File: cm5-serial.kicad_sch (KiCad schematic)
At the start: 1 part

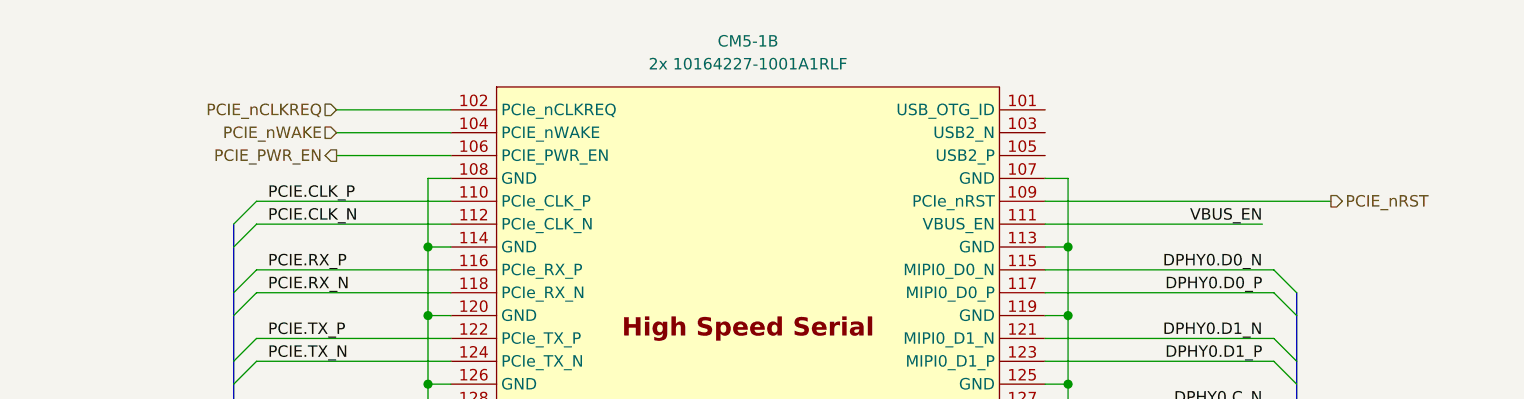
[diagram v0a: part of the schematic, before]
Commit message: abstractified pcie sideband sigs
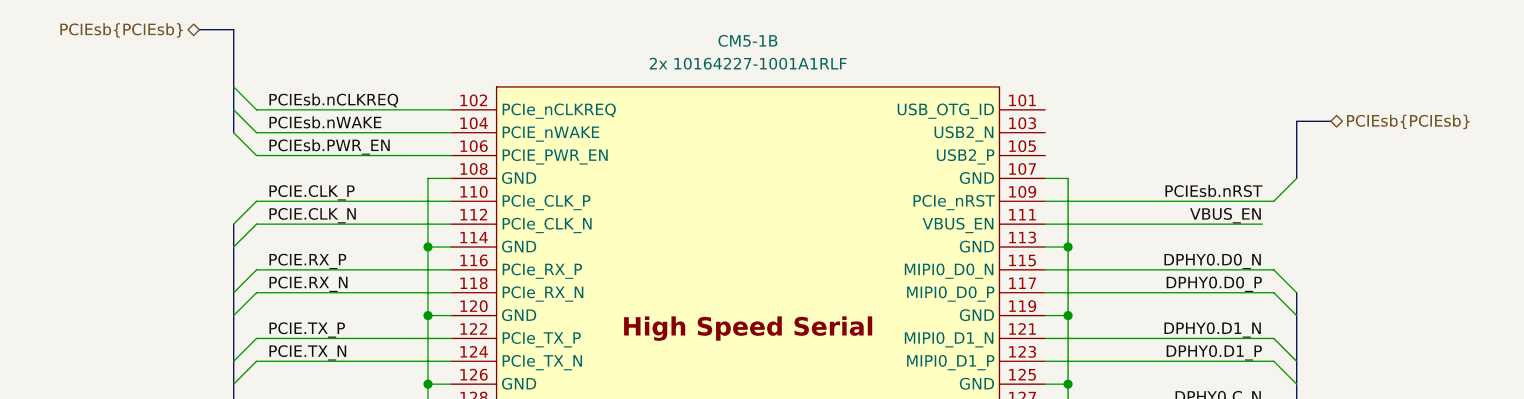
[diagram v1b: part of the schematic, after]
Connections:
- net PCIE_PWR_EN renamed PCIEsb.PWR_EN
- net PCIE_nCLKREQ renamed PCIEsb.nCLKREQ
- net PCIE_nRST renamed PCIEsb.nRST
- net PCIE_nWAKE renamed PCIEsb.nWAKE
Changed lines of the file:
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@@
 		(company "Andre S Winkel | Highlander Space Program | University of California, Riverside")
+	)
+	(bus_alias "PCIEsb"
+		(members "nCLKREQ" "nWAKE" "PWR_EN" "nRST")
 	)
 	(junction
@@
 	)
 	(bus_entry
+		(at 74.93 34.29)
+		(size 2.54 2.54)
+		(stroke
+			(width 0)
+			(type default)
+		)
+	)
+	(bus_entry
 		(at 74.93 44.45)
 		(size 2.54 -2.54)
@@
 	)
 	(bus_entry
+		(at 193.04 39.37)
+		(size -2.54 2.54)
+		(stroke
+			(width 0)
+			(type default)
+		)
+	)
+	(bus_entry
+		(at 74.93 29.21)
+		(size 2.54 2.54)
+		(stroke
+			(width 0)
+			(type default)
+		)
+	)
+	(bus_entry
 		(at 193.04 77.47)
 		(size -2.54 -2.54)
@@
 	)
 	(bus_entry
+		(at 77.47 34.29)
+		(size -2.54 -2.54)
+		(stroke
+			(width 0)
+			(type default)
+		)
+	)
+	(bus_entry
 		(at 193.04 151.13)
 		(size -2.54 -2.54)
@@
 	(wire
 		(pts
-			(xy 86.36 36.83) (xy 99.06 36.83)
-		)
-		(stroke
-			(width 0)
-			(type default)
-		)
-	)
-	(wire
-		(pts
 			(xy 167.64 62.23) (xy 167.64 54.61)
 		)
@@
 	(wire
 		(pts
+			(xy 77.47 36.83) (xy 99.06 36.83)
+		)
+		(stroke
+			(width 0)
+			(type default)
+		)
+	)
+	(wire
+		(pts
 			(xy 167.64 153.67) (xy 167.64 161.29)
 		)
@@
 		)
 	)
+	(bus
+		(pts
+			(xy 74.93 22.86) (xy 71.12 22.86)
+		)
+		(stroke
+			(width 0)
+			(type default)
+		)
+	)
 	(wire
 		(pts
@@
 	(bus
 		(pts
+			(xy 193.04 33.02) (xy 193.04 39.37)
+		)
+		(stroke
+			(width 0)
+			(type default)
+		)
+	)
+	(bus
+		(pts
 			(xy 74.93 54.61) (xy 74.93 52.07)
 		)
@@
 	(wire
 		(pts
-			(xy 86.36 34.29) (xy 99.06 34.29)
-		)
-		(stroke
-			(width 0)
-			(type default)
-		)
-	)
-	(wire
-		(pts
 			(xy 167.64 107.95) (xy 167.64 115.57)
 		)
@@
 	(bus
 		(pts
+			(xy 196.85 33.02) (xy 193.04 33.02)
+		)
+		(stroke
+			(width 0)
+			(type default)
+		)
+	)
+	(bus
+		(pts
+			(xy 74.93 29.21) (xy 74.93 31.75)
+		)
+		(stroke
+			(width 0)
+			(type default)
+		)
+	)
+	(bus
+		(pts
 			(xy 193.04 74.93) (xy 193.04 69.85)
 		)
@@
 	(wire
 		(pts
-			(xy 86.36 31.75) (xy 99.06 31.75)
-		)
-		(stroke
-			(width 0)
-			(type solid)
-		)
-	)
-	(wire
-		(pts
 			(xy 165.1 59.69) (xy 190.5 59.69)
 		)
@@
 		)
 	)
+	(bus
+		(pts
+			(xy 74.93 31.75) (xy 74.93 34.29)
+		)
+		(stroke
+			(width 0)
+			(type default)
+		)
+	)
 	(wire
 		(pts
@@
 	(wire
 		(pts
+			(xy 77.47 31.75) (xy 99.06 31.75)
+		)
+		(stroke
+			(width 0)
+			(type default)
+		)
+	)
+	(wire
+		(pts
 			(xy 165.1 140.97) (xy 190.5 140.97)
 		)
@@
 		)
 	)
+	(bus
+		(pts
+			(xy 74.93 22.86) (xy 74.93 29.21)
+		)
+		(stroke
+			(width 0)
+			(type default)
+		)
+	)
 	(wire
 		(pts
@@
 	(wire
 		(pts
-			(xy 165.1 41.91) (xy 196.85 41.91)
+			(xy 165.1 41.91) (xy 190.5 41.91)
 		)
 		(stroke
@@
 		(pts
 			(xy 74.93 62.23) (xy 74.93 59.69)
+		)
+		(stroke
+			(width 0)
+			(type default)
+		)
+	)
+	(wire
+		(pts
+			(xy 77.47 34.29) (xy 99.06 34.29)
 		)
 		(stroke
@@
 		)
 	)
+	(label "PCIEsb.nWAKE"
+		(at 78.74 34.29 0)
+		(effects
+			(font
+				(size 1.27 1.27)
+			)
+			(justify left bottom)
+		)
+	)
 	(label "DPHY1.D2_P"
 		(at 189.23 151.13 180)
@@
 		)
 	)
+	(label "PCIEsb.nCLKREQ"
+		(at 78.74 31.75 0)
+		(effects
+			(font
+				(size 1.27 1.27)
+			)
+			(justify left bottom)
+		)
+	)
+	(label "PCIEsb.nRST"
+		(at 189.23 41.91 180)
+		(effects
+			(font
+				(size 1.27 1.27)
+			)
+			(justify right bottom)
+		)
+	)
 	(label "DPHY1.C_P"
 		(at 189.23 143.51 180)
@@
 		)
 	)
+	(label "PCIEsb.PWR_EN"
+		(at 78.74 36.83 0)
+		(effects
+			(font
+				(size 1.27 1.27)
+			)
+			(justify left bottom)
+		)
+	)
 	(label "PCIE.TX_N"
 		(at 78.74 59.69 0)
@@
 		)
 	)
-	(hierarchical_label "PCIE_nWAKE"
-		(shape input)
-		(at 86.36 34.29 180)
-		(effects
-			(font
-				(size 1.27 1.27)
-			)
-			(justify right)
-		)
-	)
-	(hierarchical_label "PCIE_PWR_EN"
-		(shape output)
-		(at 86.36 36.83 180)
-		(effects
-			(font
-				(size 1.27 1.27)
-			)
-			(justify right)
+	(hierarchical_label "PCIEsb{PCIEsb}"
+		(shape bidirectional)
+		(at 196.85 33.02 0)
+		(effects
+			(font
+				(size 1.27 1.27)
+			)
+			(justify left)
 		)
 	)
@@
 		)
 	)
-	(hierarchical_label "PCIE_nCLKREQ"
-		(shape input)
-		(at 86.36 31.75 180)
-		(effects
-			(font
-				(size 1.27 1.27)
-			)
-			(justify right)
-		)
-	)
-	(hierarchical_label "PCIE_nRST"
-		(shape output)
-		(at 196.85 41.91 0)
-		(effects
-			(font
-				(size 1.27 1.27)
-			)
-			(justify left)
-		)
-	)
 	(hierarchical_label "DPHY0{DPHY}"
 		(shape bidirectional)
@@
 		)
 	)
+	(hierarchical_label "PCIEsb{PCIEsb}"
+		(shape bidirectional)
+		(at 71.12 22.86 180)
+		(effects
+			(font
+				(size 1.27 1.27)
+			)
+			(justify right)
+		)
+	)

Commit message: neo m8m impl.
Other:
- note added: "what is vbus en"
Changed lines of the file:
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@@
 		(members "nCLKREQ" "nWAKE" "PWR_EN" "nRST")
+	)
+	(text "what is vbus en\n"
+		(exclude_from_sim no)
+		(at 234.95 59.69 0)
+		(effects
+			(font
+				(size 2.54 2.54)
+			)
+		)
 	)
 	(junction
@@
 		(on_board yes)
 		(dnp no)
-		(property "Reference" "#PWR02"
+		(property "Reference" "#PWR04"
 			(at 167.64 167.64 0)
 			(effects
@@
 			(project "CUTIE-CITRUS"
 				(path "/40af415e-5e3a-41a5-ab07-08c2181863e4/0ab77a57-2cdd-42e3-9db1-21e8f0163da9/a16d2f87-5159-48aa-a50b-c816b9ab5677"
-					(reference "#PWR02")
+					(reference "#PWR04")
 					(unit 1)
 				)
@@
 		(on_board yes)
 		(dnp no)
-		(property "Reference" "#PWR01"
+		(property "Reference" "#PWR03"
 			(at 96.52 167.64 0)
 			(effects
@@
 			(project "CUTIE-CITRUS"
 				(path "/40af415e-5e3a-41a5-ab07-08c2181863e4/0ab77a57-2cdd-42e3-9db1-21e8f0163da9/a16d2f87-5159-48aa-a50b-c816b9ab5677"
-					(reference "#PWR01")
+					(reference "#PWR03")
 					(unit 1)
 				)

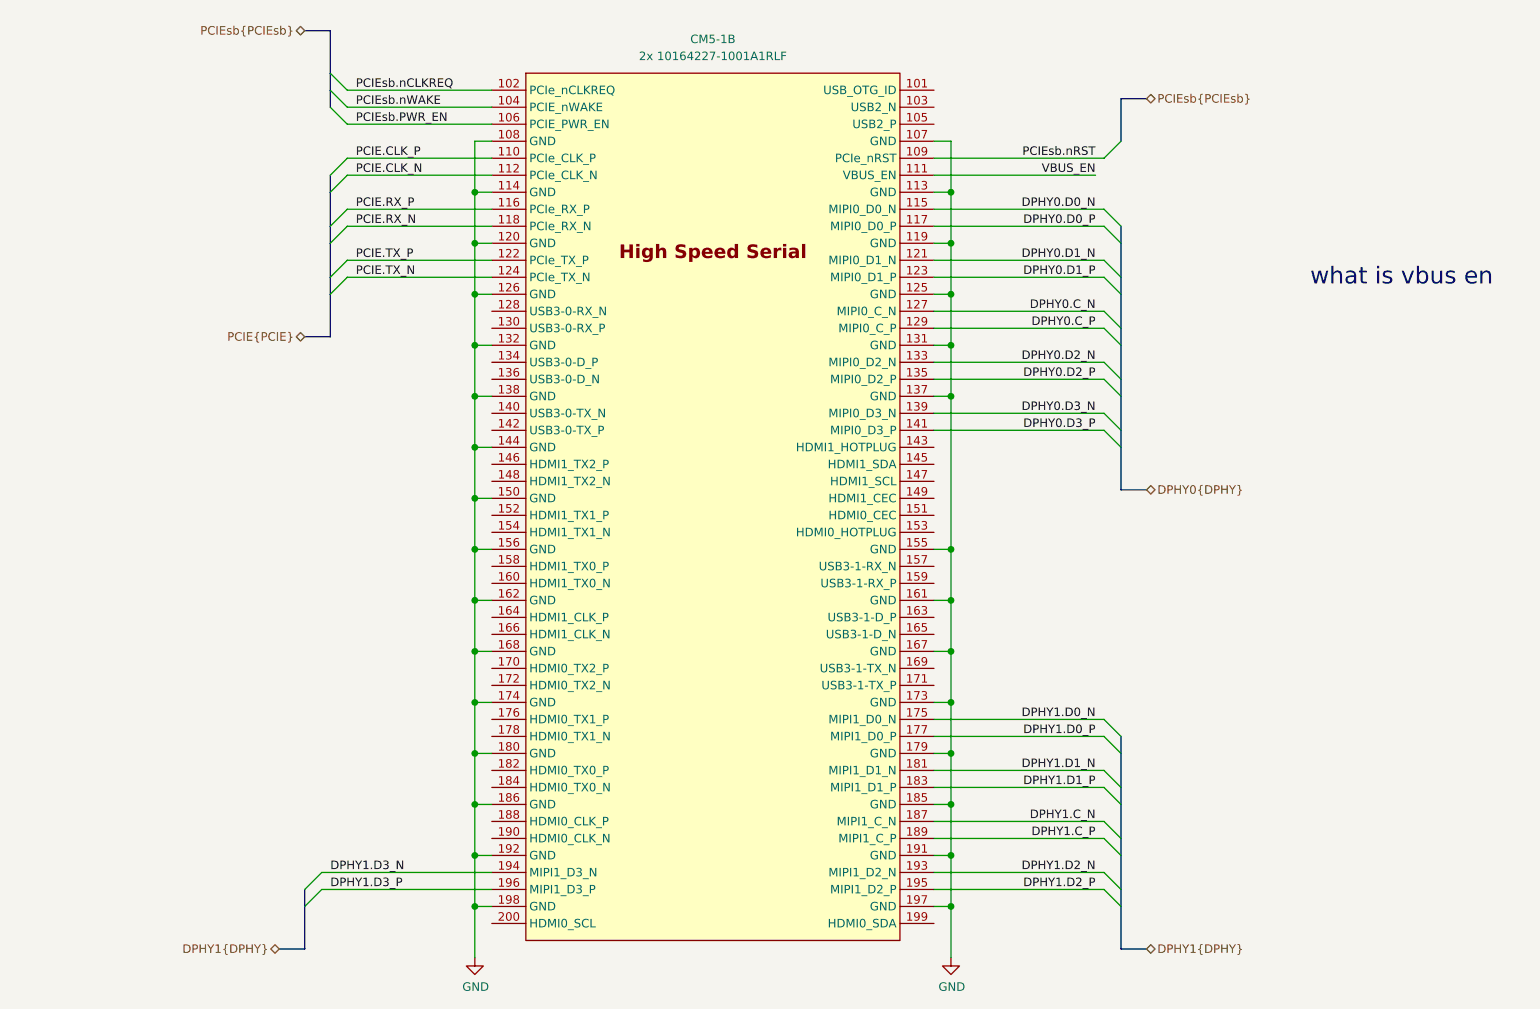
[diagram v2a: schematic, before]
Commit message: prepared usb3, abstracted cameras, backplane connector
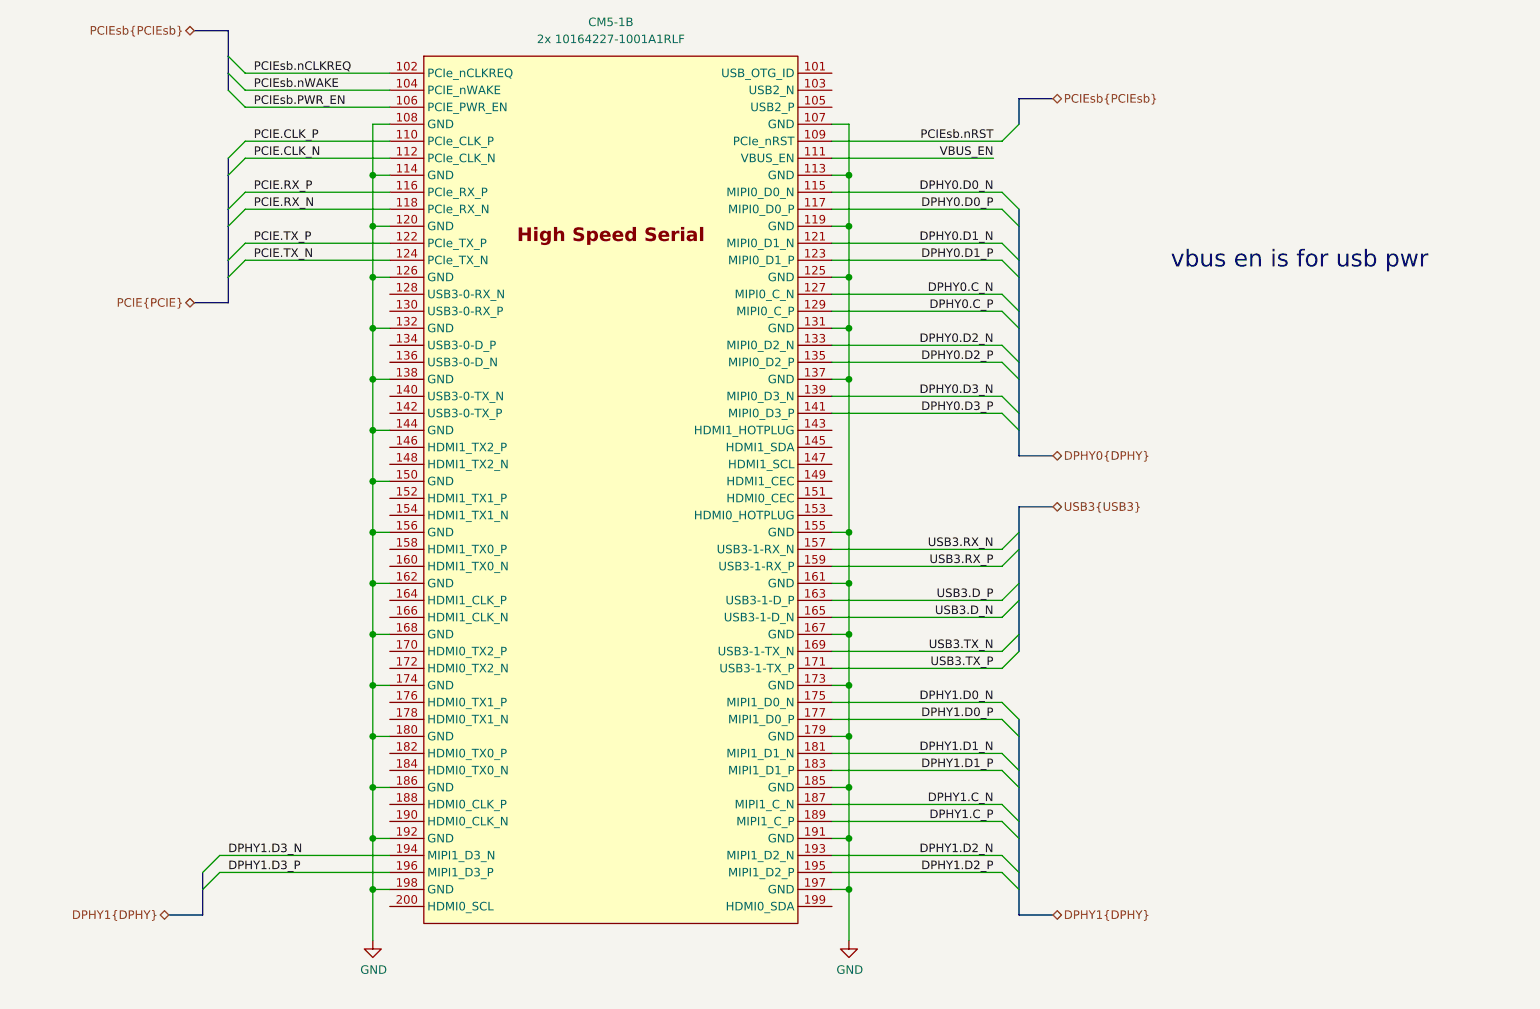
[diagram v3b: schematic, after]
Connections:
- net USB3.RX_N: now reaches CM5-1.157 (USB3-1-RX_N)
- net USB3.RX_P: now reaches CM5-1.159 (USB3-1-RX_P)
- net USB3.D_P: now reaches CM5-1.163 (USB3-1-D_P)
- net USB3.D_N: now reaches CM5-1.165 (USB3-1-D_N)
- net USB3.TX_N: now reaches CM5-1.169 (USB3-1-TX_N)
- net USB3.TX_P: now reaches CM5-1.171 (USB3-1-TX_P)
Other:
- note added: "vbus en is for usb pwr"
- note removed: "what is vbus en"
- moved on the sheet: CM5-1B

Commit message: un-abstraction, footprints, layout edge cuts
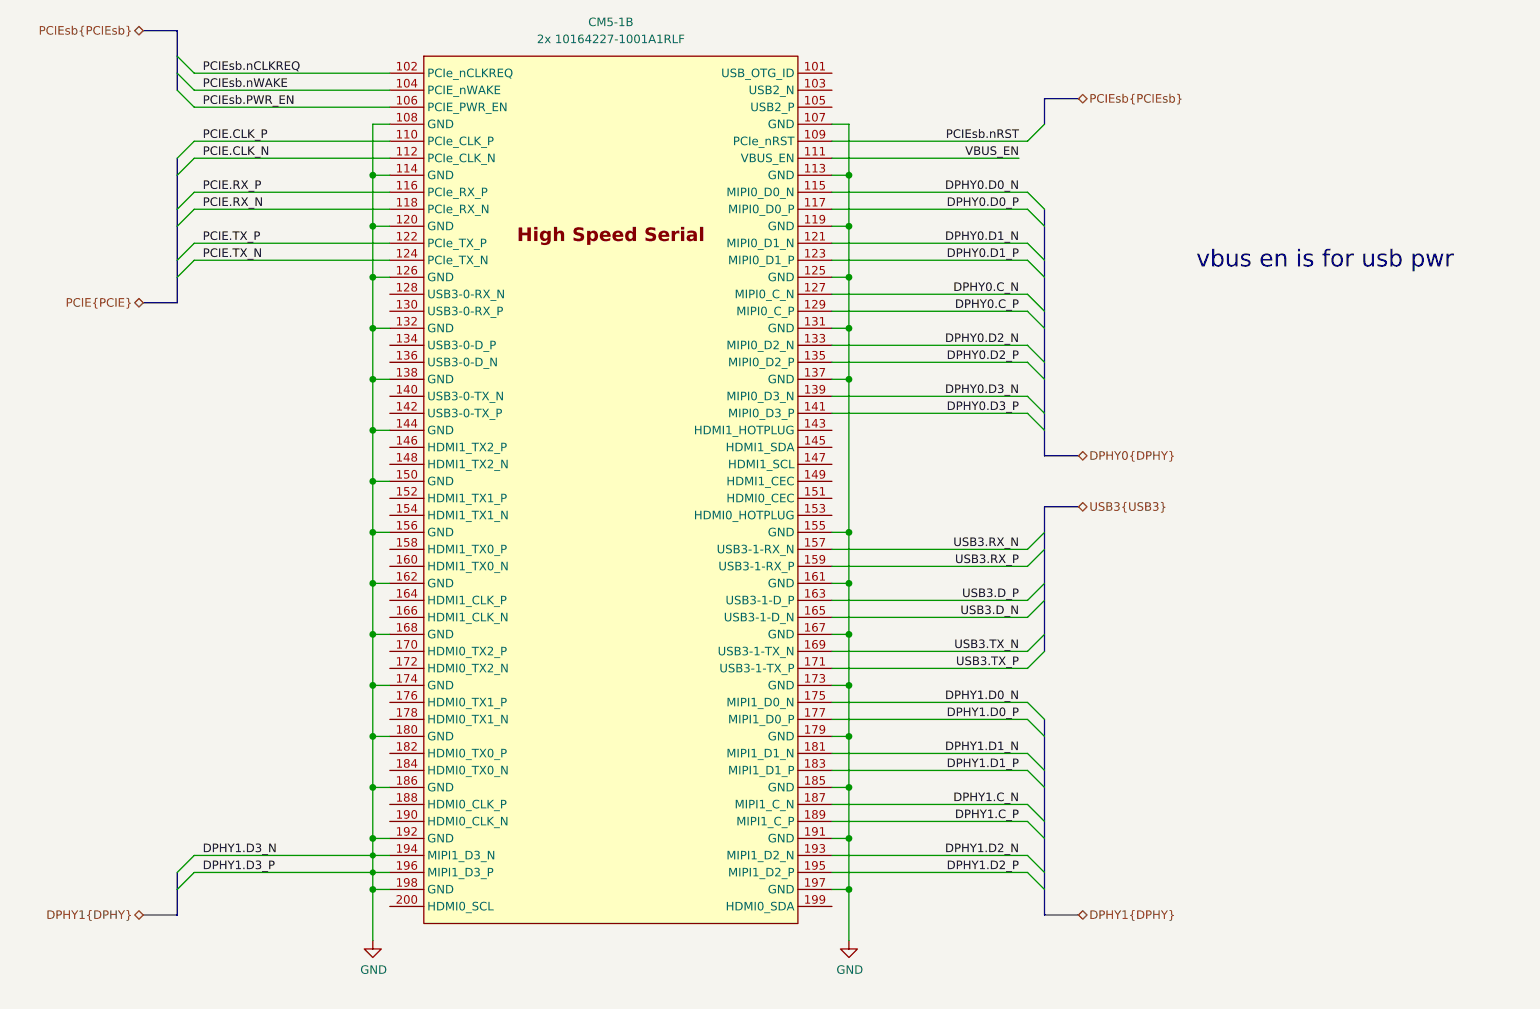
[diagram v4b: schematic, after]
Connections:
- net DPHY1.D3_N is gone; now on net GND: CM5-1.194 (MIPI1_D3_N)
- net DPHY1.D3_P is gone; now on net GND: CM5-1.196 (MIPI1_D3_P)

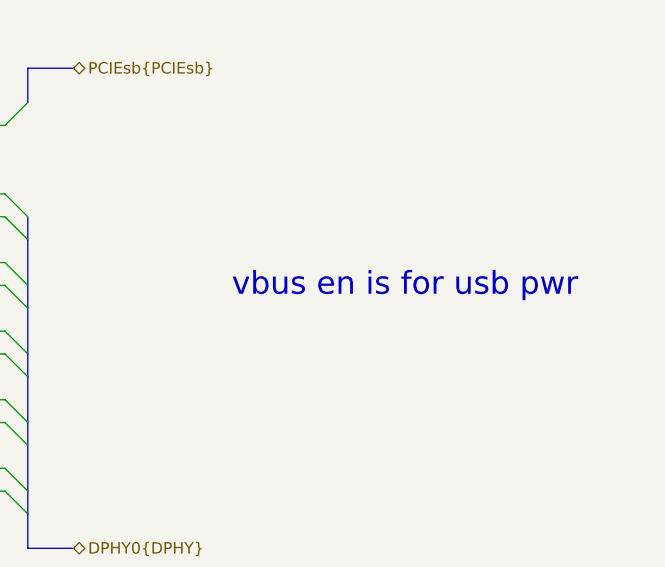
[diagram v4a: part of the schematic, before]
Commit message: removed ublox
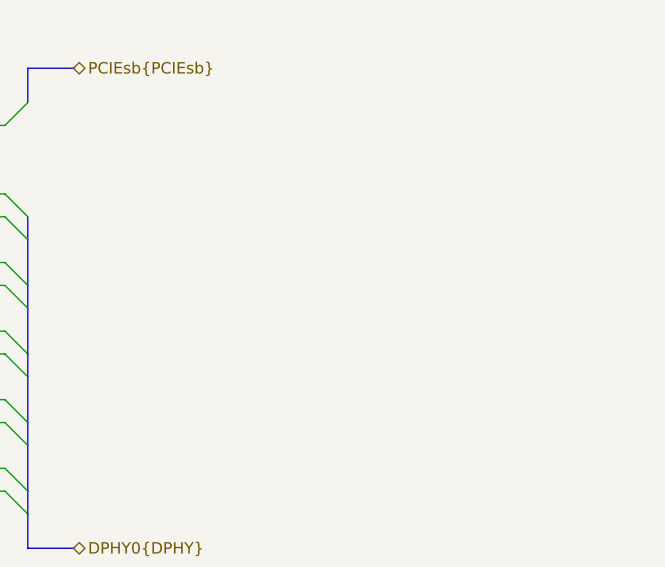
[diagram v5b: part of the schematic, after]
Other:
- note removed: "vbus en is for usb pwr"
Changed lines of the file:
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@@
 		(members "D_N" "D_P" "RX_N" "RX_P" "TX_N" "TX_P")
-	)
-	(text "vbus en is for usb pwr"
-		(exclude_from_sim no)
-		(at 223.52 57.15 0)
-		(effects
-			(font
-				(size 2.54 2.54)
-			)
-		)
 	)
 	(junction

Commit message: starting layout
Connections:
- net GND: no longer CM5-1.194 (MIPI1_D3_N), CM5-1.196 (MIPI1_D3_P)
- net USB3.D_N: now also CM5-1.136 (USB3-0-D_N); no longer CM5-1.165 (USB3-1-D_N)
- net USB3.D_P: now also CM5-1.134 (USB3-0-D_P); no longer CM5-1.163 (USB3-1-D_P)
- net USB3.RX_N: now also CM5-1.128 (USB3-0-RX_N); no longer CM5-1.157 (USB3-1-RX_N)
- net USB3.RX_P: now also CM5-1.130 (USB3-0-RX_P); no longer CM5-1.159 (USB3-1-RX_P)
- net USB3.TX_N: now also CM5-1.140 (USB3-0-TX_N); no longer CM5-1.169 (USB3-1-TX_N)
- net USB3.TX_P: now also CM5-1.142 (USB3-0-TX_P); no longer CM5-1.171 (USB3-1-TX_P)
- new net DPHY1.D3_N: CM5-1.194 (MIPI1_D3_N)
- new net DPHY1.D3_P: CM5-1.196 (MIPI1_D3_P)
